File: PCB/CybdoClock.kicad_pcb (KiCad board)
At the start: 2 copper layers, 155 x 155 mm, 237 parts, among them Q1 CJL2301, Q10 HSW6822, Q11 HSW6822, Q12 HSW6822, Q13 HSW6822, Q14 HSW6822, Q2 CJL2301, Q3 CJL2301, Q4 CJL2301, Q5 CJL2301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

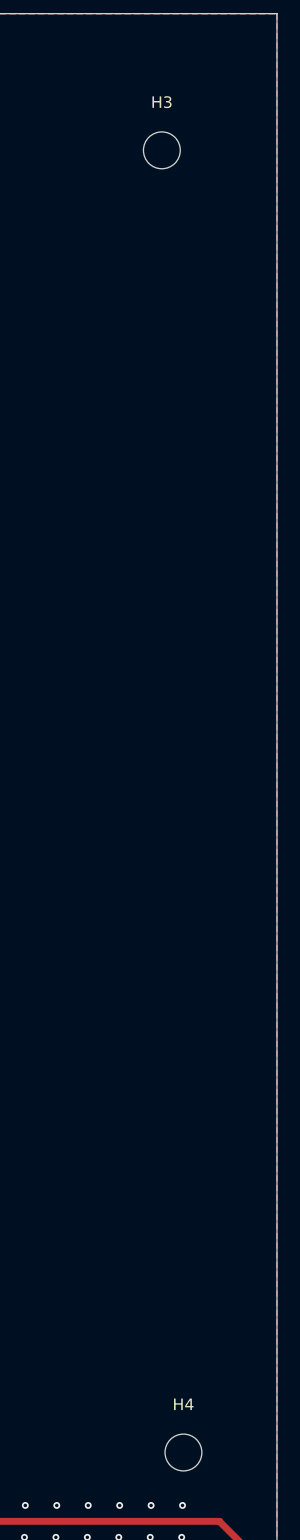
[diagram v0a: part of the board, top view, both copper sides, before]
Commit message: updated mounting holes and some 3d models
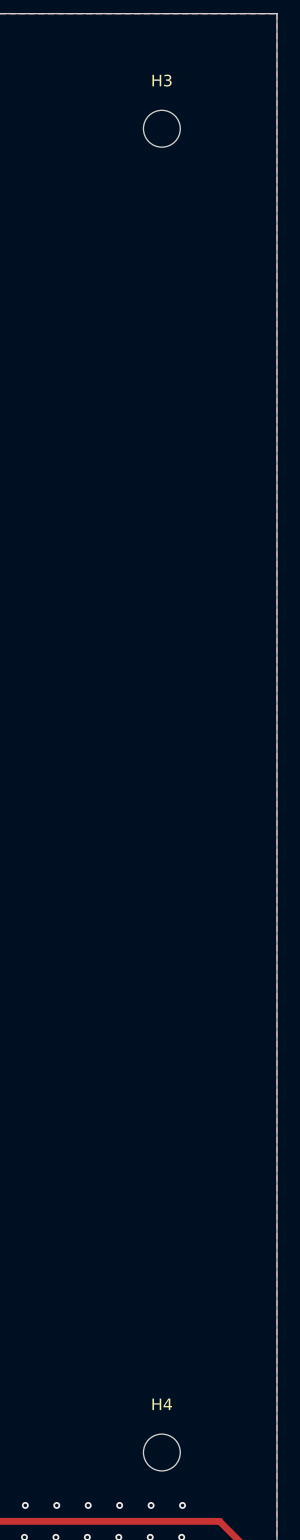
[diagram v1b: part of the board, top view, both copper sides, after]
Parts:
- moved H3 1.88 mm to (160.3, 47.4)
- moved H4 1.88 mm to (160.3, 162.4)

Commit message: use built in serial pins, start on firmware using circuitpython
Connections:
- U1 pad 11: unconnected-(U1-GPIO18_D10_MOSI-Pad11)_1 -> /DATA
- U1 pad 3: /DATA -> unconnected-(U1-GPIO2_A2_D2-Pad3)_1
- U1 pad 5: /CLOCK -> unconnected-(U1-GPIO22_D4_SDA-Pad5)
- U1 pad 9: unconnected-(U1-GPIO19_D8_SCK-Pad9)_1 -> /CLOCK
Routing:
- net /ADC_ALS: track 4.28 -> 55.7 mm
- net /CLOCK: track 240.1 -> 243.9 mm
- net /DATA: track 50.8 -> 48.5 mm, vias 0 -> 1
- net +3V3: track 59.4 -> 58.5 mm
- net GND: vias 189 -> 191
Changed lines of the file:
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@@
 			(layers "*.Cu" "*.Mask")
 			(remove_unused_layers no)
-			(net "/DATA")
+			(net "unconnected-(U1-GPIO2_A2_D2-Pad3)")
 			(pinfunction "GPIO2_A2_D2_3")
-			(pintype "passive")
+			(pintype "passive+no_connect")
 		)
 		(pad "3" smd roundrect
@@
 			(layers "B.Cu" "B.Mask")
 			(roundrect_rratio 0.1)
-			(net "/DATA")
+			(net "unconnected-(U1-GPIO2_A2_D2-Pad3)_1")
 			(pinfunction "GPIO2_A2_D2_3")
-			(pintype "passive")
+			(pintype "passive+no_connect")
 			(thermal_bridge_angle 45)
 		)
@@
 			(layers "*.Cu" "*.Mask")
 			(remove_unused_layers no)
-			(net "/CLOCK")
+			(net "unconnected-(U1-GPIO22_D4_SDA-Pad5)_1")
 			(pinfunction "GPIO22_D4_SDA_5")
-			(pintype "passive")
+			(pintype "passive+no_connect")
 		)
 		(pad "5" smd roundrect
@@
 			(layers "B.Cu" "B.Mask")
 			(roundrect_rratio 0.1)
-			(net "/CLOCK")
+			(net "unconnected-(U1-GPIO22_D4_SDA-Pad5)")
 			(pinfunction "GPIO22_D4_SDA_5")
-			(pintype "passive")
+			(pintype "passive+no_connect")
 			(thermal_bridge_angle 45)
 		)
@@
 			(layers "B.Cu" "B.Mask")
 			(roundrect_rratio 0.1)
-			(net "unconnected-(U1-GPIO19_D8_SCK-Pad9)")
+			(net "/CLOCK")
 			(pinfunction "GPIO19_D8_SCK_9")
-			(pintype "passive+no_connect")
+			(pintype "passive")
 			(thermal_bridge_angle 45)
 		)
@@
 			(layers "*.Cu" "*.Mask")
 			(remove_unused_layers no)
-			(net "unconnected-(U1-GPIO19_D8_SCK-Pad9)_1")
+			(net "/CLOCK")
 			(pinfunction "GPIO19_D8_SCK_9")
-			(pintype "passive+no_connect")
+			(pintype "passive")
 		)
 		(pad "10" smd roundrect
@@
 			(layers "B.Cu" "B.Mask")
 			(roundrect_rratio 0.1)
-			(net "unconnected-(U1-GPIO18_D10_MOSI-Pad11)")
+			(net "/DATA")
 			(pinfunction "GPIO18_D10_MOSI_11")
-			(pintype "passive+no_connect")
+			(pintype "passive")
 			(thermal_bridge_angle 45)
 		)
@@
 			(layers "*.Cu" "*.Mask")
 			(remove_unused_layers no)
-			(net "unconnected-(U1-GPIO18_D10_MOSI-Pad11)_1")
+			(net "/DATA")
 			(pinfunction "GPIO18_D10_MOSI_11")
-			(pintype "passive+no_connect")
+			(pintype "passive")
 		)
 		(pad "12" smd roundrect
@@
 	)
 	(via
+		(at 163.44 185.14)
+		(size 0.6)
+		(drill 0.3)
+		(layers "F.Cu" "B.Cu")
+		(free yes)
+		(net "GND")
+	)
+	(via
 		(at 85.87 181.13)
 		(size 0.6)
@@
 	)
 	(via
+		(at 161.41 185.14)
+		(size 0.6)
+		(drill 0.3)
+		(layers "F.Cu" "B.Cu")
+		(free yes)
+		(net "GND")
+	)
+	(via
 		(at 26.67 163.77)
 		(size 0.6)
@@
 	)
 	(segment
+		(start 165.998949 187.281051)
+		(end 120.908949 187.281051)
+		(width 0.2)
+		(layer "F.Cu")
+		(net "/ADC_ALS")
+	)
+	(segment
+		(start 120.038949 188.151051)
+		(end 116.868949 188.151051)
+		(width 0.2)
+		(layer "F.Cu")
+		(net "/ADC_ALS")
+	)
+	(segment
+		(start 120.908949 187.281051)
+		(end 120.038949 188.151051)
+		(width 0.2)
+		(layer "F.Cu")
+		(net "/ADC_ALS")
+	)
+	(segment
 		(start 116.923949 185.021051)
 		(end 116.923949 188.096051)
@@
 	)
 	(segment
+		(start 167.368949 188.651051)
+		(end 165.998949 187.281051)
+		(width 0.2)
+		(layer "F.Cu")
+		(net "/ADC_ALS")
+	)
+	(segment
 		(start 37.483949 142.836051)
 		(end 37.478949 142.841051)
@@
 	)
 	(segment
-		(start 162.288949 181.921051)
+		(start 162.288949 180.95)
+		(end 156.357898 186.881051)
+		(width 0.2)
+		(layer "F.Cu")
+		(net "+3V3")
+	)
+	(segment
+		(start 162.288949 180.95)
 		(end 162.288949 173.411051)
 		(width 0.2)
@@
 	)
 	(segment
-		(start 162.448949 182.081051)
-		(end 162.288949 181.921051)
+		(start 156.357898 186.881051)
+		(end 119.95 186.881051)
 		(width 0.2)
 		(layer "F.Cu")
@@
 	)
 	(via
-		(at 162.448949 182.081051)
+		(at 119.95 186.881051)
 		(size 0.6)
 		(drill 0.3)
@@
 	)
 	(segment
-		(start 115.598949 186.881051)
-		(end 157.648949 186.881051)
-		(width 0.2)
-		(layer "B.Cu")
-		(net "+3V3")
-	)
-	(segment
-		(start 157.648949 186.881051)
-		(end 162.448949 182.081051)
+		(start 119.95 186.881051)
+		(end 115.598949 186.881051)
 		(width 0.2)
 		(layer "B.Cu")
@@
 	)
 	(segment
-		(start 157.208949 188.651051)
-		(end 151.618949 183.061051)
+		(start 154.668949 173.411051)
+		(end 154.668949 181.436736)
 		(width 0.2)
 		(layer "F.Cu")
@@
 	)
 	(segment
-		(start 151.618949 183.061051)
-		(end 112.838949 183.061051)
+		(start 20.088949 89.331051)
+		(end 18.908949 89.331051)
 		(width 0.2)
 		(layer "F.Cu")
@@
 	)
 	(segment
-		(start 20.088949 89.331051)
-		(end 18.908949 89.331051)
+		(start 22.048948 89.331051)
+		(end 20.088949 89.331051)
 		(width 0.2)
 		(layer "F.Cu")
@@
 	)
 	(segment
-		(start 22.048948 89.331051)
-		(end 20.088949 89.331051)
+		(start 153.044634 183.061051)
+		(end 112.838949 183.061051)
 		(width 0.2)
 		(layer "F.Cu")
@@
 		(net "/CLOCK")
 	)
+	(segment
+		(start 154.668949 181.436736)
+		(end 153.044634 183.061051)
+		(width 0.2)
+		(layer "F.Cu")
+		(net "/CLOCK")
+	)
 	(via
 		(at 67.968949 183.061051)
@@
 	)
 	(segment
-		(start 159.748949 188.651051)
-		(end 153.318949 182.221051)
-		(width 0.2)
-		(layer "F.Cu")
-		(net "/LATCH")
-	)
-	(segment
 		(start 114.12301 178.011051)
 		(end 114.12301 182.18699)
@@
 	)
 	(segment
-		(start 153.318949 182.221051)
-		(end 114.088949 182.221051)
-		(width 0.2)
-		(layer "F.Cu")
-		(net "/LATCH")
-	)
-	(segment
 		(start 69.24301 182.215112)
 		(end 69.248949 182.221051)
@@
 	)
 	(segment
+		(start 159.748949 188.651051)
+		(end 153.708949 182.611051)
+		(width 0.2)
+		(layer "B.Cu")
+		(net "/LATCH")
+	)
+	(segment
 		(start 18.078949 135.421051)
 		(end 18.078949 92.201051)
@@
 	)
 	(segment
+		(start 153.708949 182.611051)
+		(end 118.291051 182.611051)
+		(width 0.2)
+		(layer "B.Cu")
+		(net "/LATCH")
+	)
+	(segment
 		(start 43.438949 182.221051)
 		(end 18.078949 156.861051)
@@
 	)
 	(segment
+		(start 118.291051 182.611051)
+		(end 117.901051 182.221051)
+		(width 0.2)
+		(layer "B.Cu")
+		(net "/LATCH")
+	)
+	(segment
+		(start 117.901051 182.221051)
+		(end 114.088949 182.221051)
+		(width 0.2)
+		(layer "B.Cu")
+		(net "/LATCH")
+	)
+	(segment
 		(start 72.537898 179.9)
 		(end 108.424061 179.9)
@@
 	)
 	(segment
-		(start 154.948949 181.311051)
+		(start 126.958949 181.311051)
 		(end 118.688949 181.311051)
 		(width 0.2)
@@
 	)
 	(segment
+		(start 127.54 180.73)
+		(end 126.958949 181.311051)
+		(width 0.2)
+		(layer "F.Cu")
+		(net "/DATA")
+	)
+	(segment
 		(start 118.688949 181.311051)
 		(end 116.66301 179.285112)
@@
 		(net "/DATA")
 	)
+	(via
+		(at 127.54 180.73)
+		(size 0.6)
+		(drill 0.3)
+		(layers "F.Cu" "B.Cu")
+		(net "/DATA")
+	)
 	(segment
-		(start 162.288949 188.651051)
-		(end 154.948949 181.311051)
+		(start 127.56 180.75)
+		(end 127.54 180.73)
 		(width 0.2)
-		(layer "F.Cu")
+		(layer "B.Cu")
+		(net "/DATA")
+	)
+	(segment
+		(start 152.41 180.75)
+		(end 127.56 180.75)
+		(width 0.2)
+		(layer "B.Cu")
+		(net "/DATA")
+	)
+	(segment
+		(start 159.748949 173.411051)
+		(end 152.41 180.75)
+		(width 0.2)
+		(layer "B.Cu")
 		(net "/DATA")
 	)

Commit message: firmware done, centered leds positioning
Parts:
- moved D1 2.00 mm to (42.9, 67.4)
- moved D10 2.00 mm to (42.9, 134.7)
- moved D100 2.00 mm to (95.2, 74.9)
- moved D101 2.00 mm to (95.2, 82.4)
- moved D102 2.00 mm to (95.2, 89.8)
- moved D103 2.00 mm to (95.2, 97.3)
- moved D104 2.00 mm to (95.2, 104.8)
- moved D105 2.00 mm to (95.2, 112.2)
- moved D106 2.00 mm to (95.2, 119.7)
- moved D107 2.00 mm to (95.2, 127.2)
- moved D108 2.00 mm to (95.2, 134.7)
- moved D109 2.00 mm to (95.2, 142.1)
- moved D11 2.00 mm to (42.9, 142.1)
- moved D110 2.00 mm to (95.2, 149.6)
- moved D111 2.00 mm to (95.2, 157.1)
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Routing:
- net Net-(U4-QH'): track 77.6 -> 41.2 mm
- net /LATCH: track 236.5 -> 232.6 mm
- net /CLOCK: track 243.9 -> 240.0 mm
- net GND: track 112.2 -> 109.8 mm, vias 191 -> 197
- net /ROW2: track 21.8 -> 24.1 mm
- net Net-(U3-QH'): track 73.8 -> 71.8 mm
- net /ROW7: track 26.1 -> 24.7 mm
- net /ROW14: track 26.6 -> 25.2 mm
- net Net-(U2-QH'): track 40.8 -> 41.9 mm
- net /ROW1: track 22.8 -> 23.7 mm, vias 0 -> 2
- net /ROW5: track 6.17 -> 5.34 mm
- net /ROW11: track 7.81 -> 7.03 mm
- net /ROW3: track 10.5 -> 9.75 mm
- net /ROW9: track 9.16 -> 8.51 mm
- net /DATA: track 48.5 -> 47.9 mm
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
